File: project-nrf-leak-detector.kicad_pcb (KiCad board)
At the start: 2 copper layers, 51.3 x 36.8 mm, 18 parts, among them J1 Conn_02x05_Odd_Even, J2 Water Probe, Q1 Q_NMOS_GSD, U1 MS88SF3_NRF52840

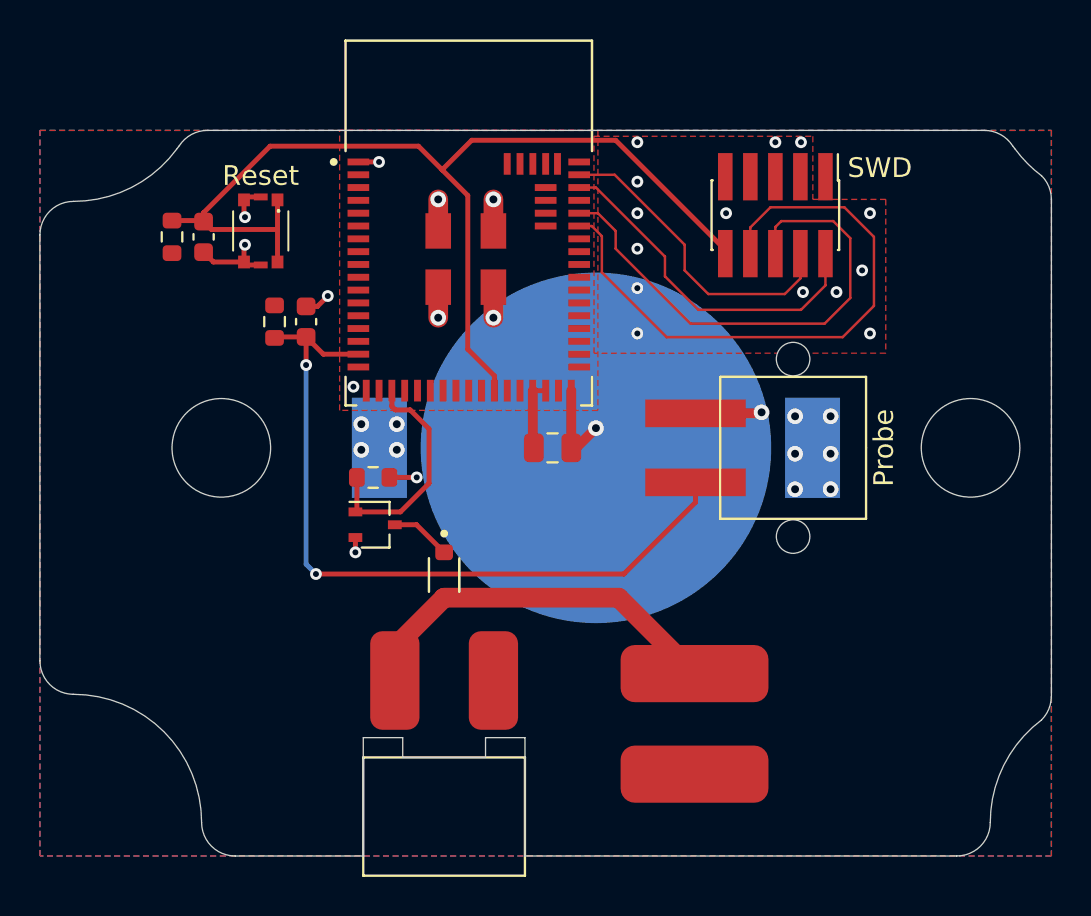
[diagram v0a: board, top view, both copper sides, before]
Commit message: Update to KiCAD 7.0
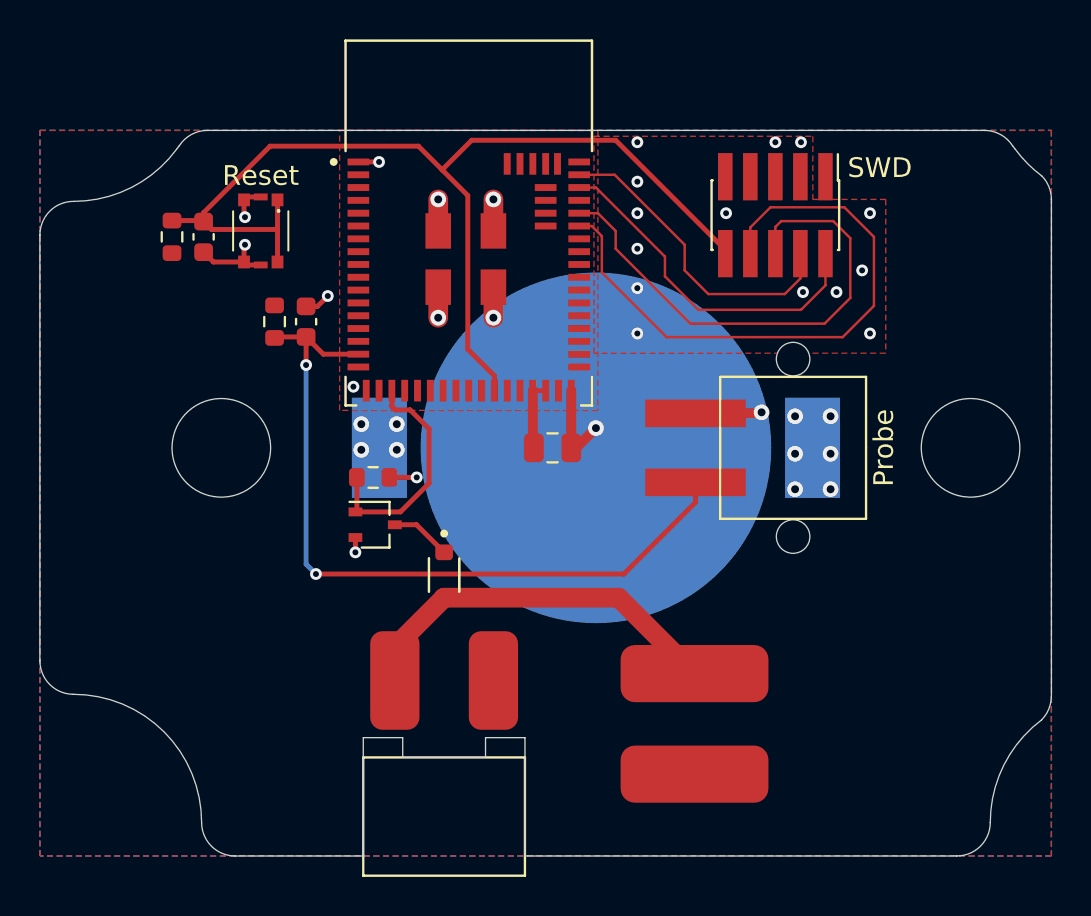
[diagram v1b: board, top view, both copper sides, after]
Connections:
- net /~RESET renamed /~{RESET}
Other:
- net class Default removed
